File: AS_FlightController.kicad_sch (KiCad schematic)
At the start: 42 parts, among them J1 USB_C_Receptacle_USB2.0, SW1 SW_SPDT, U1 STM32H753ZIT6, U2 AMS1117-3.3, U3 USBLC6-2SC6, Y1 25MHZ, Y2 32.67 KHz

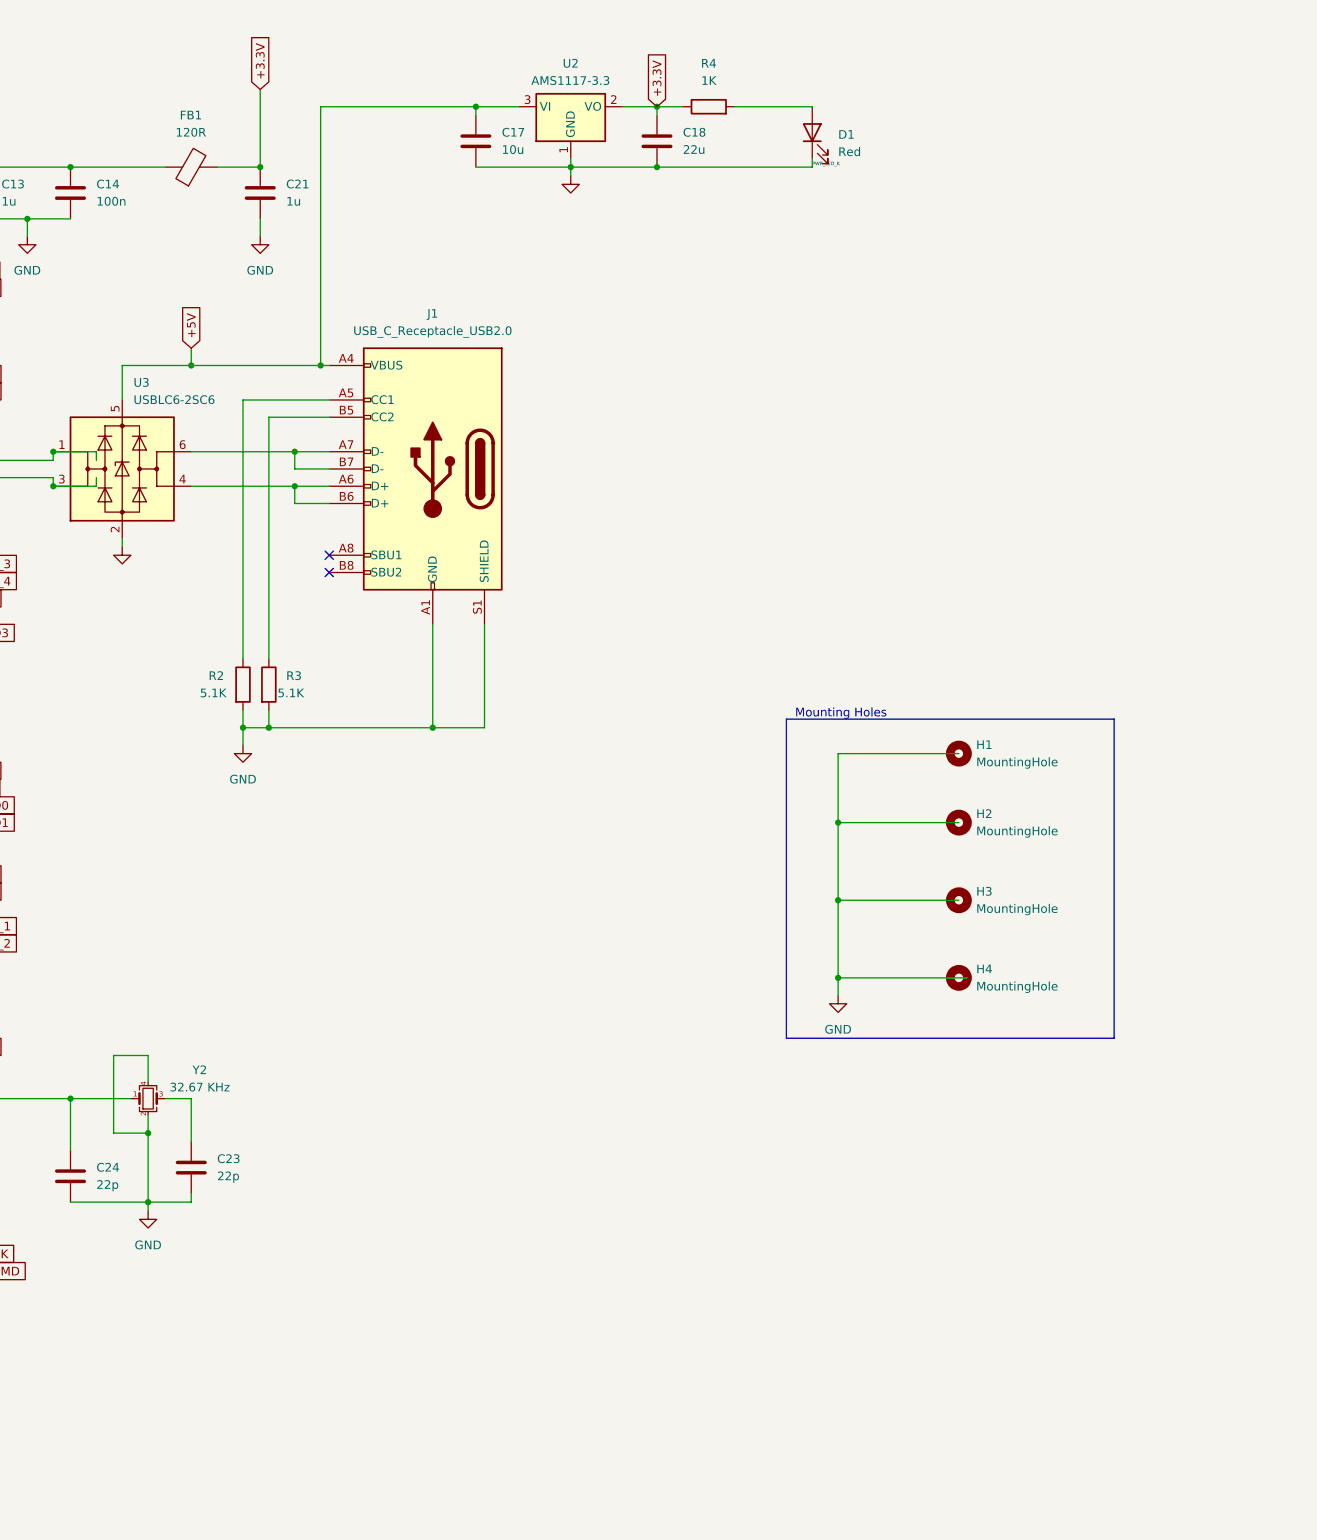
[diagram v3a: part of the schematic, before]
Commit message: Added peripherals
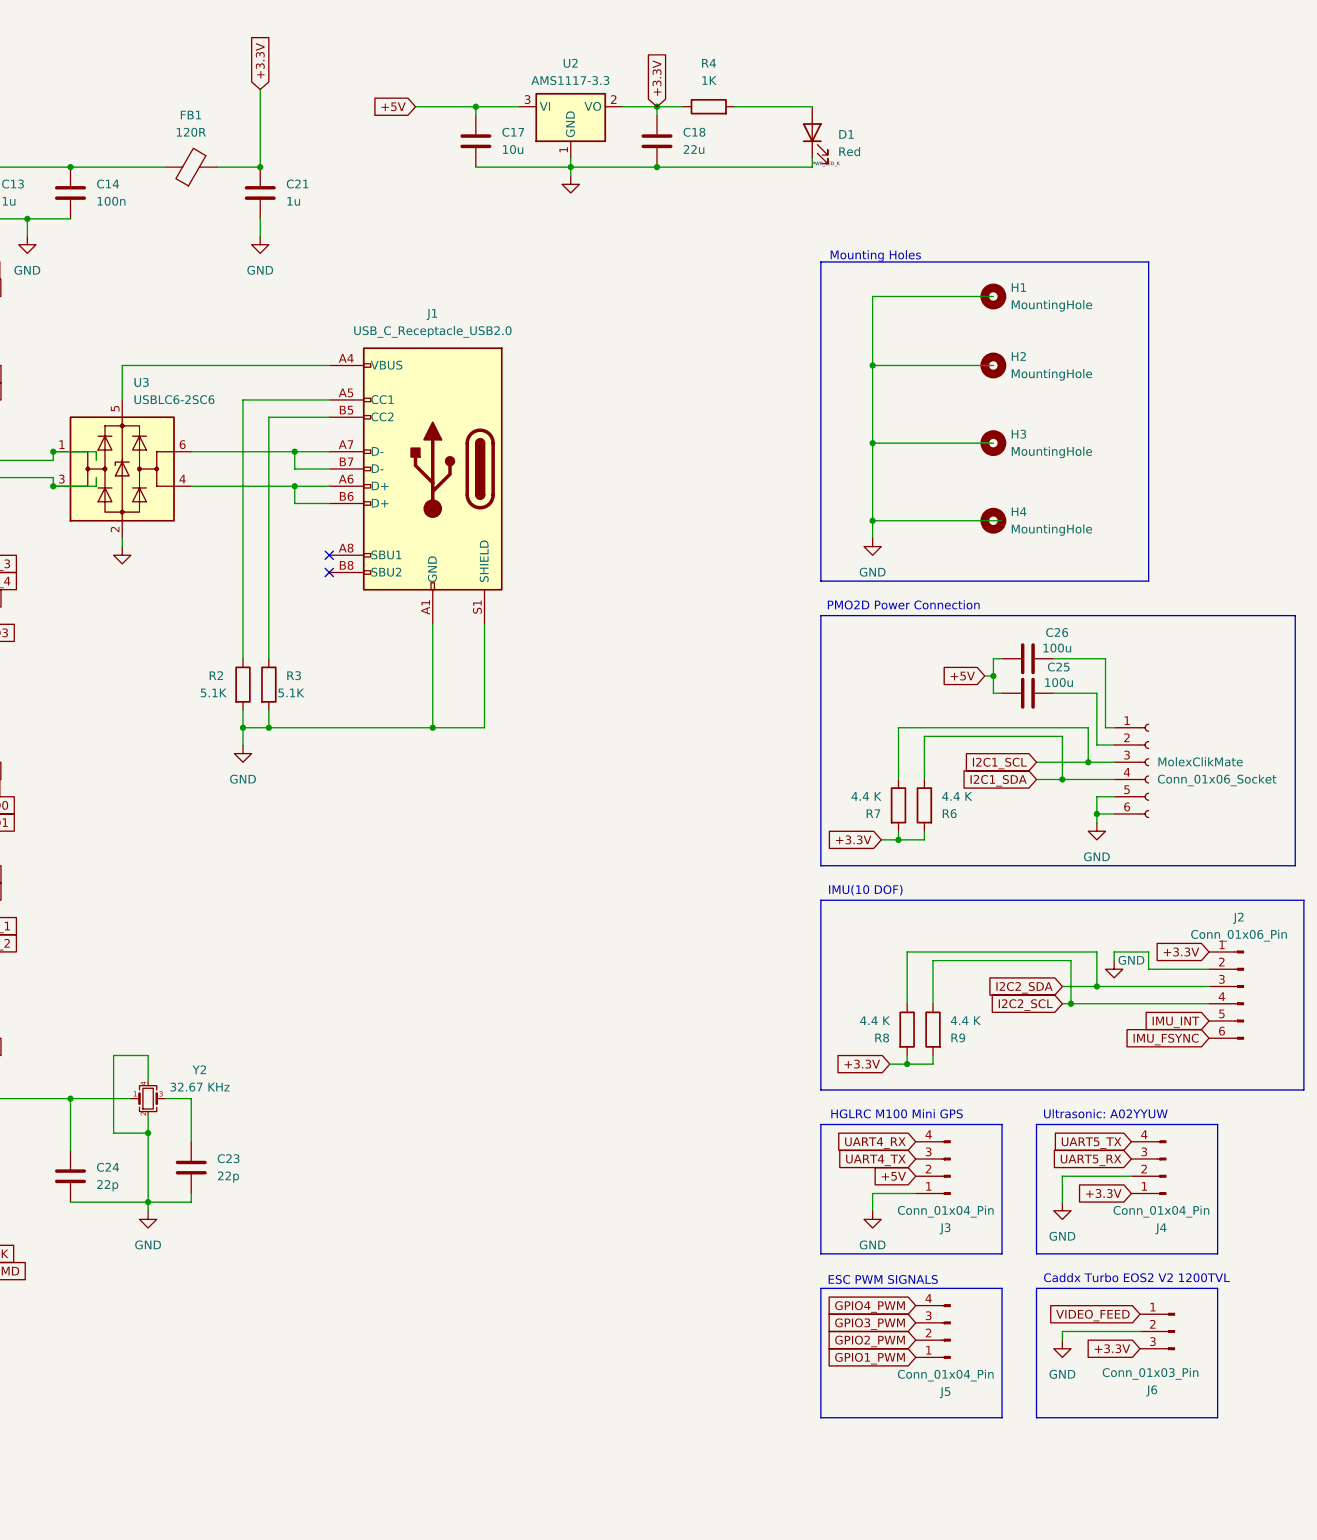
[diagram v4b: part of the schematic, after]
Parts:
- added C25, C26: 100u, symbol Device:C
- added J2: Conn_01x06_Pin, symbol Connector:Conn_01x06_Pin
- added J3, J4, J5: Conn_01x04_Pin, symbol Connector:Conn_01x04_Pin
- added J6: Conn_01x03_Pin, symbol Connector:Conn_01x03_Pin
- added MolexClikMate: Conn_01x06_Socket, MolexCLIK-Mate, symbol Connector:Conn_01x06_Socket
- added R6, R7, R8, R9: 4.4 K, symbol Device:R
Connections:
- net +3.3V: now also J2.1 (Pin_1), J4.1 (Pin_1), J6.3 (Pin_3), R6.2, R7.2, R8.2, R9.2
- net +5V: now also C25.1, C26.1, J3.2 (Pin_2); no longer J1.A4 (VBUS), J1.A9 (VBUS), J1.B4 (VBUS), J1.B9 (VBUS), U3.5 (VBUS)
- net GND: now also J2.2 (Pin_2), J3.1 (Pin_1), J4.2 (Pin_2), J6.2 (Pin_2), MolexClikMate.5 (Pin_5), MolexClikMate.6 (Pin_6)
- net I2C1_SCL: now also MolexClikMate.3 (Pin_3), R7.1
- net I2C1_SDA: now also MolexClikMate.4 (Pin_4), R6.1
- net I2C2_SCL: now also J2.4 (Pin_4), R9.1
- net I2C2_SDA: now also J2.3 (Pin_3), R8.1
- net UART4_RX: now also J3.4 (Pin_4)
- net UART4_TX: now also J3.3 (Pin_3)
- net UART5_RX: now also J4.3 (Pin_3)
- net UART5_TX: now also J4.4 (Pin_4)
- new net: C26.2, MolexClikMate.1 (Pin_1)
- new net: C25.2, MolexClikMate.2 (Pin_2)
- new net: J1.A4 (VBUS), J1.A9 (VBUS), J1.B4 (VBUS), J1.B9 (VBUS), U3.5 (VBUS)
- new net GPIO1_PWM: J5.1 (Pin_1)
- new net GPIO2_PWM: J5.2 (Pin_2)
- new net GPIO3_PWM: J5.3 (Pin_3)
- new net GPIO4_PWM: J5.4 (Pin_4)
- new net IMU_FSYNC: J2.6 (Pin_6)
- new net IMU_INT: J2.5 (Pin_5)
- new net VIDEO_FEED: J6.1 (Pin_1)
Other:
- note added: "Caddx Turbo EOS2 V2 1200TVL"
- note added: "ESC PWM SIGNALS"
- note added: "HGLRC M100 Mini GPS"
- note added: "IMU(10 DOF)"
- note added: "PMO2D Power Connection"
- note added: "Ultrasonic: A02YYUW"
- moved on the sheet: H1, H2, H3, H4
